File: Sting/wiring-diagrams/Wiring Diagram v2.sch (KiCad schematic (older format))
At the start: 31 parts

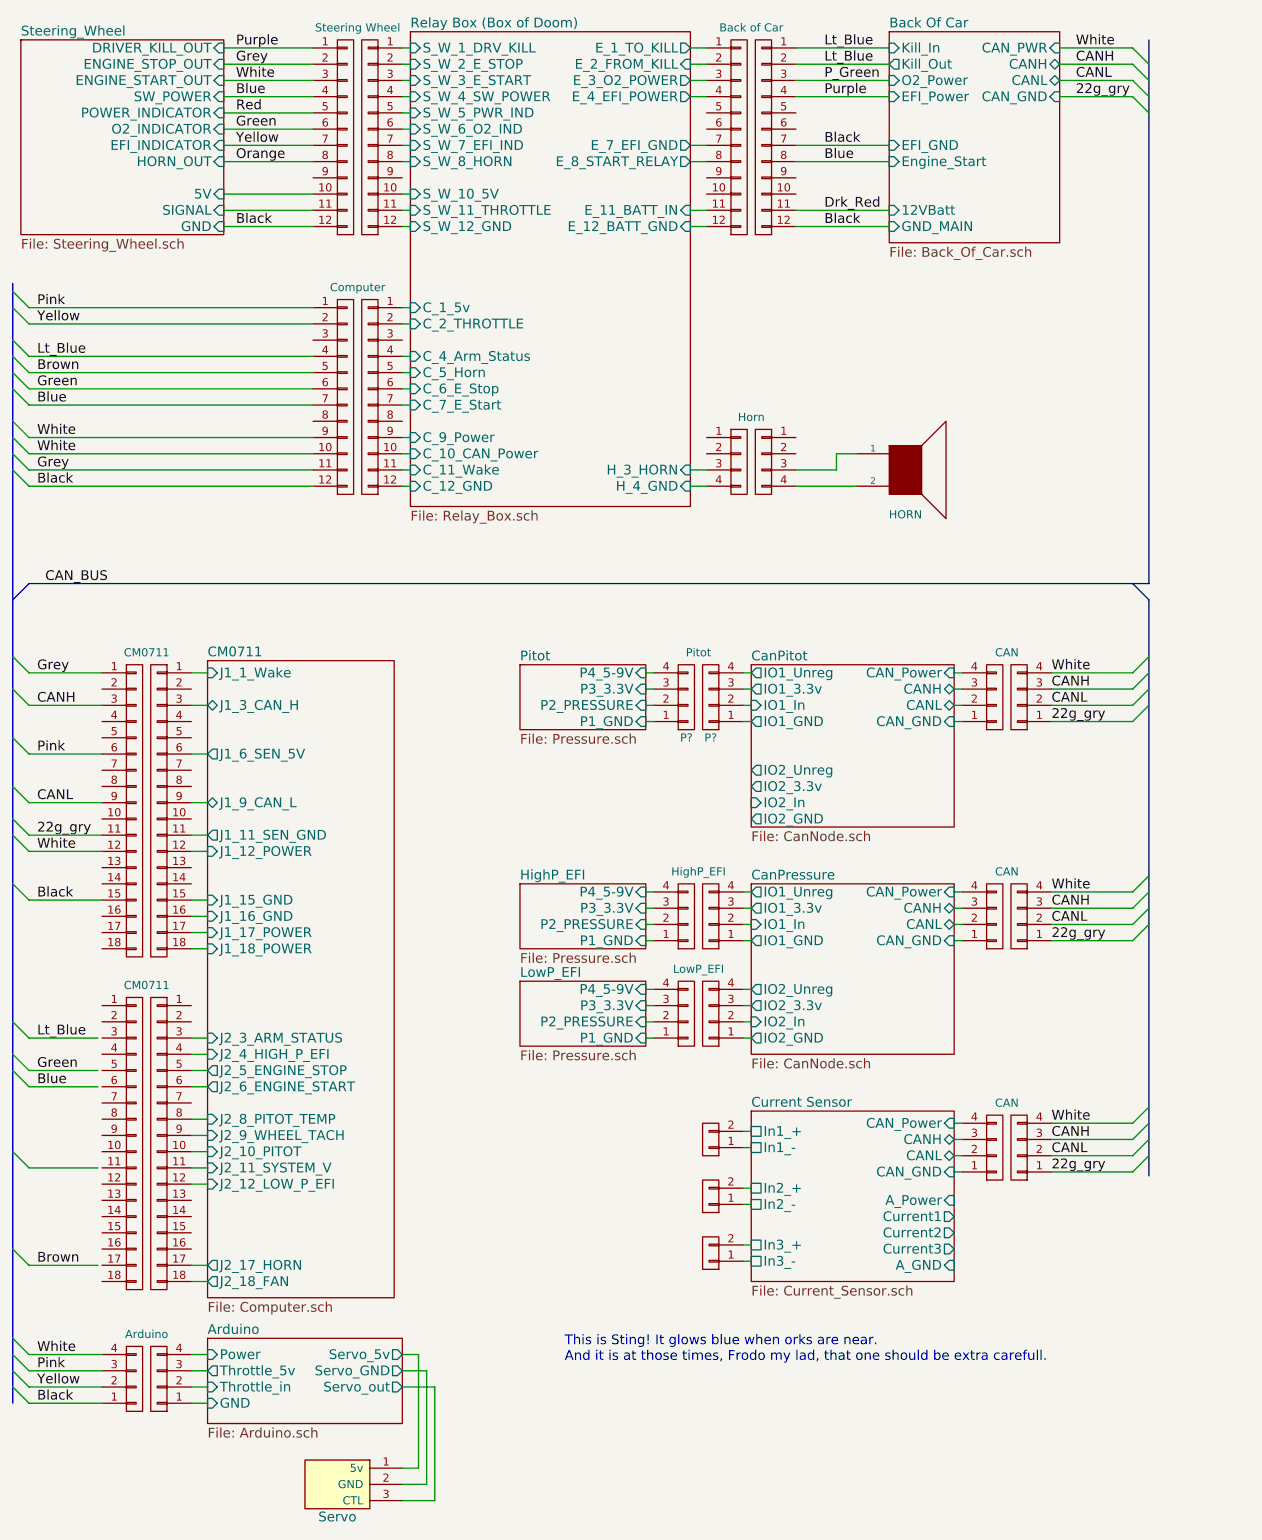
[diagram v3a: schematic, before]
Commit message: Added 12v regulator, minor formatting mistakes.
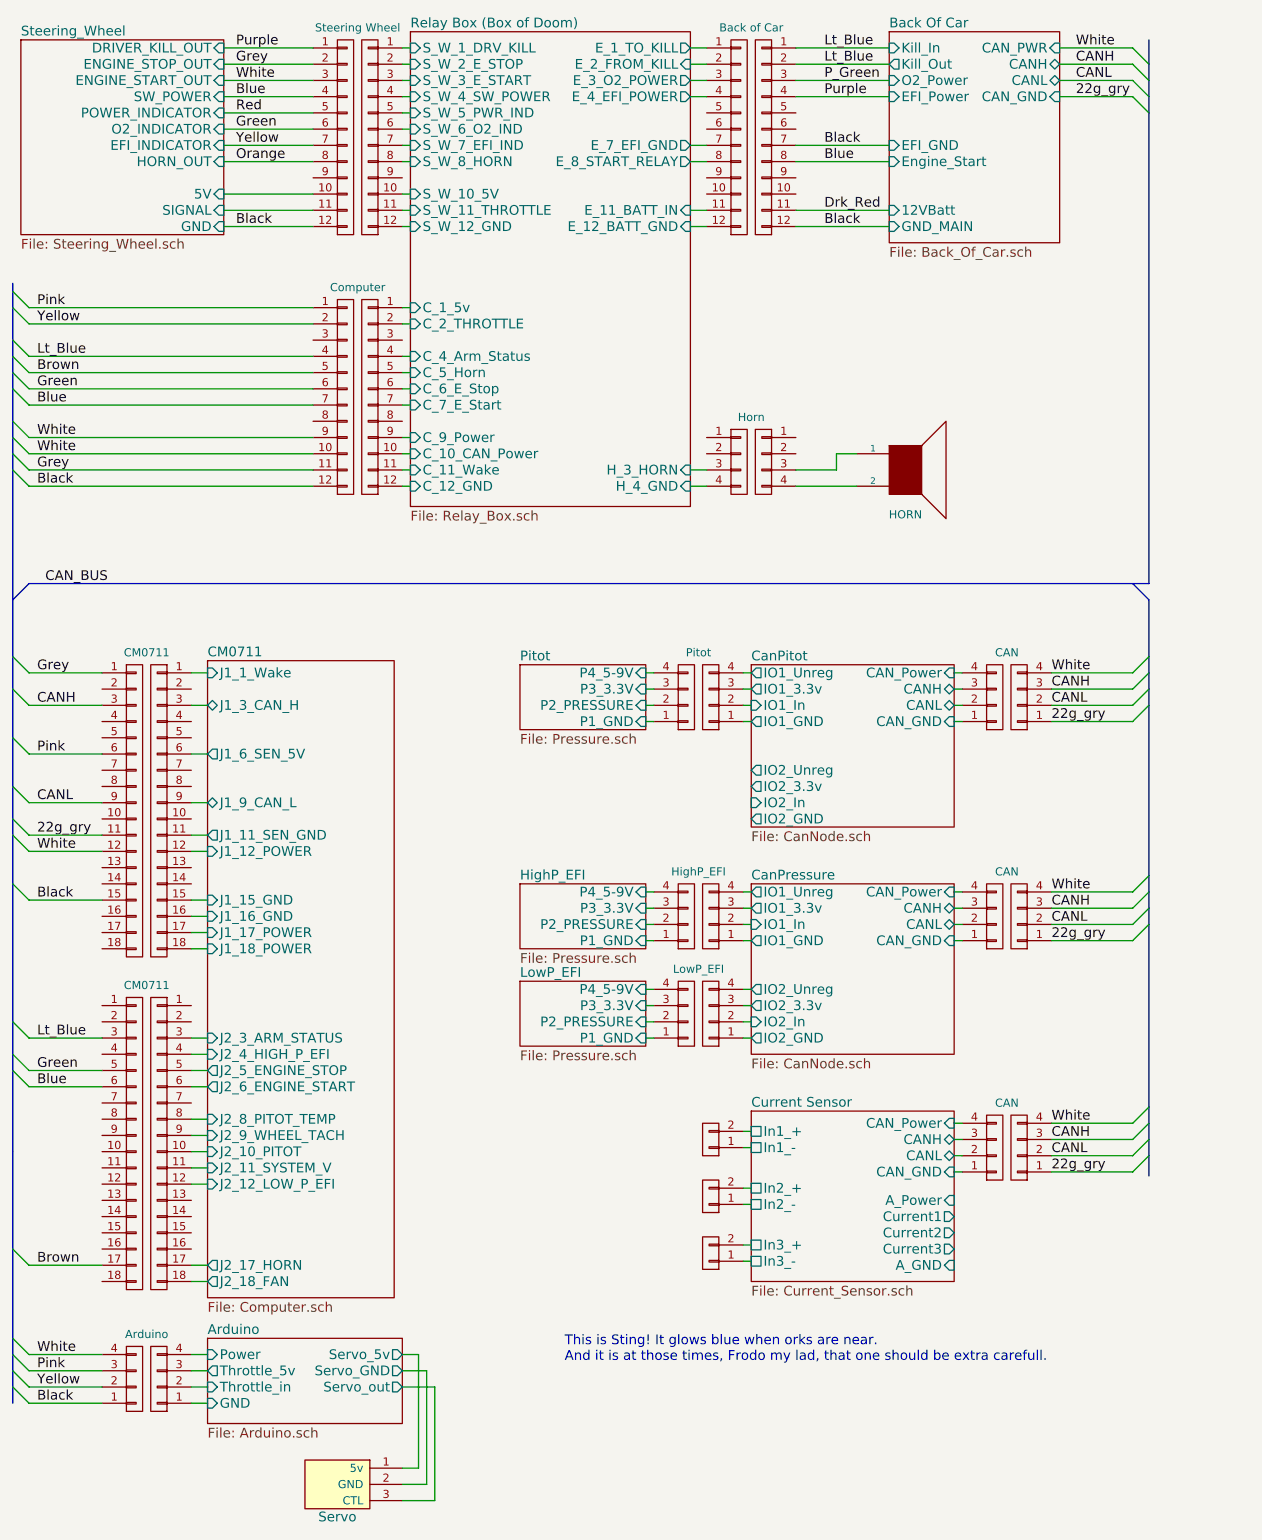
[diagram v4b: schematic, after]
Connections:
- net Blue: now also P?.6 (P6)
- net Brown: now also P?.17 (P17)
- net Green: now also P?.5 (P5)
- net Lt_Blue: now also P?.3 (P3)
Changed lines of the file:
@@
 	800  7400 900  7500
-Entry Wire Line
-	800  7900 900  8000
 Entry Wire Line
 	800  8500 900  8600
@@
 	5625 3700 5875 3700
 Wire Bus Line
-	800  2550 800  9450
+	800  2550 800  2600
+Wire Bus Line
+	800  2600 800  2700
+Wire Bus Line
+	800  2700 800  2900
+Wire Bus Line
+	800  2900 800  3000
+Wire Bus Line
+	800  3000 800  3100
+Wire Bus Line
+	800  3100 800  3200
+Wire Bus Line
+	800  3200 800  3400
+Wire Bus Line
+	800  3400 800  3500
+Wire Bus Line
+	800  3500 800  3600
+Wire Bus Line
+	800  3600 800  3700
+Wire Bus Line
+	800  3700 800  4500
+Wire Bus Line
+	800  4500 800  4850
+Wire Bus Line
+	800  4850 800  5050
+Wire Bus Line
+	800  5050 800  5350
+Wire Bus Line
+	800  5350 800  5650
+Wire Bus Line
+	800  5650 800  5850
+Wire Bus Line
+	800  5850 800  5950
+Wire Bus Line
+	800  5950 800  6250
+Wire Bus Line
+	800  6250 800  7100
+Wire Bus Line
+	800  7100 800  7300
+Wire Bus Line
+	800  7300 800  7400
+Wire Bus Line
+	800  7400 800  7900
+Wire Bus Line
+	800  7900 800  8500
+Wire Bus Line
+	800  8500 800  9050
+Wire Bus Line
+	800  9050 800  9150
+Wire Bus Line
+	800  9150 800  9250
+Wire Bus Line
+	800  9250 800  9350
+Wire Bus Line
+	800  9350 800  9450
 Wire Wire Line
 	1350 4950 900  4950
@@
 	1350 6350 900  6350
 Wire Wire Line
-	1325 7200 900  7200
-Wire Wire Line
-	1325 7400 900  7400
-Wire Wire Line
-	1325 7500 900  7500
-Wire Wire Line
-	1325 8000 900  8000
-Wire Wire Line
-	1325 8600 900  8600
+	1350 7200 900  7200
+Wire Wire Line
+	1350 7400 900  7400
+Wire Wire Line
+	1350 7500 900  7500
+Wire Wire Line
+	1350 8600 900  8600
 Wire Wire Line
 	2650 2700 900  2700
@@
 	800  4500 900  4400
 Wire Bus Line
-	7800 4400 900  4400
-Wire Bus Line
-	7800 1050 7800 4400
+	7800 4400 7700 4400
+Wire Bus Line
+	7700 4400 900  4400
+Wire Bus Line
+	7800 1050 7800 1200
+Wire Bus Line
+	7800 1200 7800 1300
+Wire Bus Line
+	7800 1300 7800 1400
+Wire Bus Line
+	7800 1400 7800 1500
+Wire Bus Line
+	7800 1500 7800 4400
 Wire Wire Line
 	5625 1300 6200 1300
@@
 	7700 4400 7800 4500
 Wire Bus Line
-	7800 4500 7800 8050
+	7800 4500 7800 4850
+Wire Bus Line
+	7800 4850 7800 4950
+Wire Bus Line
+	7800 4950 7800 5050
+Wire Bus Line
+	7800 5050 7800 5150
+Wire Bus Line
+	7800 5150 7800 6200
+Wire Bus Line
+	7800 6200 7800 6300
+Wire Bus Line
+	7800 6300 7800 6400
+Wire Bus Line
+	7800 6400 7800 6500
+Wire Bus Line
+	7800 6500 7800 7625
+Wire Bus Line
+	7800 7625 7800 7725
+Wire Bus Line
+	7800 7725 7800 7825
+Wire Bus Line
+	7800 7825 7800 7925
+Wire Bus Line
+	7800 7925 7800 8050
 Wire Wire Line
 	7700 4950 7200 4950
@@
 U 1 1 58841380
 P 4950 5100
-F 0 "P?" H 4950 5350 50  0000 C CNN
+F 0 "P?" H 4950 5350 50  0001 C CNN
 F 1 "Pitot" H 5025 4825 50  0000 C CNN
 F 2 "" H 4950 5100 50  0000 C CNN
@@
 U 1 1 5884291A
 P 5100 5100
-F 0 "P?" H 5100 5350 50  0000 C CNN
+F 0 "P?" H 5100 5350 50  0001 C CNN
 F 1 "Pitot" V 5200 5100 50  0001 C CNN
 F 2 "" H 5100 5100 50  0000 C CNN
